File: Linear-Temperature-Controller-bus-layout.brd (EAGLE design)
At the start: 203.2 x 34.3 mm, 78 parts, among them IC1 LM393D, IC3 AD5624R, IC4 AD5262, IC5 LF356MX, T1 MMBT3904, T2 MMBT3904

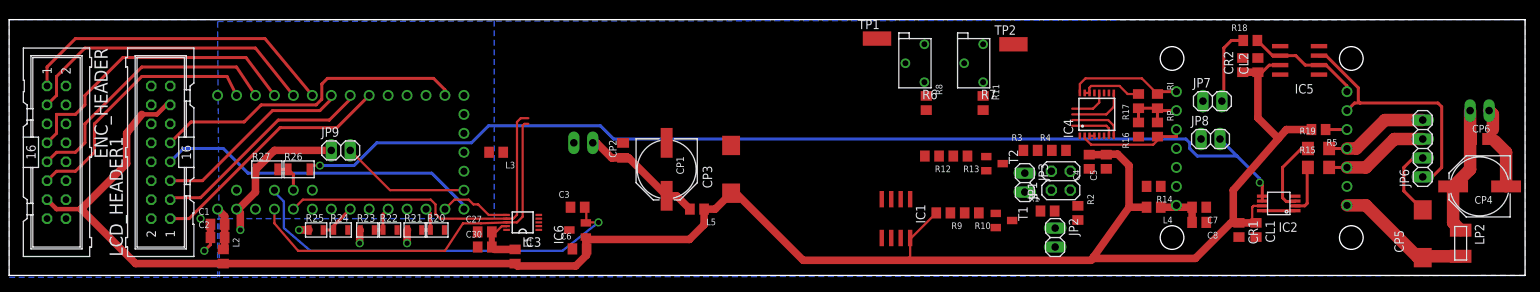
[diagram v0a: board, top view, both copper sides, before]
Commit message: Update BOM, continue laying out board
Also add a new board file to play around with having a bus of traces for
eventually extending the circuit to 4 channels
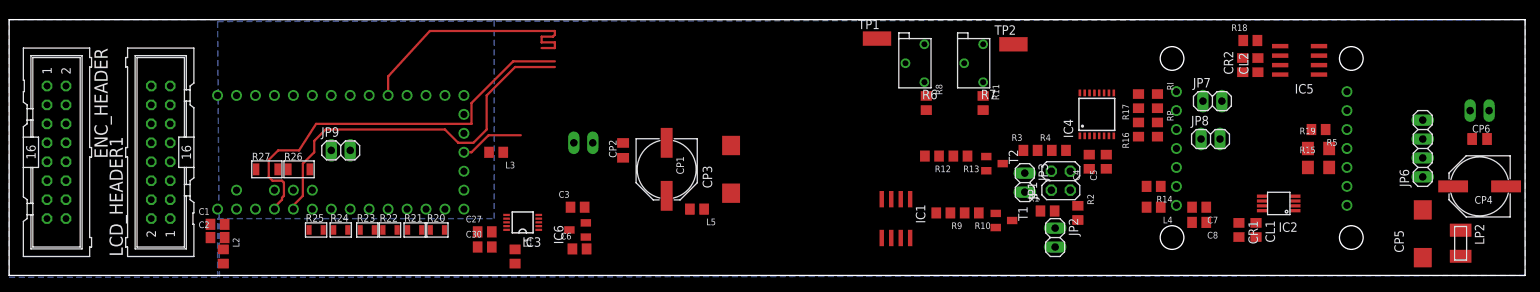
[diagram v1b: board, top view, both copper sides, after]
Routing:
- net VDD: track 267.0 -> 0.00 mm
- net VMON1: track 139.7 -> 0.00 mm, vias 2 -> 0
- net 2.5V: track 58.5 -> 0.00 mm, vias 1 -> 0
- net AGND: track 47.7 -> 0.00 mm, vias 4 -> 0
- net SCK: track 43.8 -> 0.00 mm
- net ENC_A2: track 43.2 -> 0.00 mm
- net MOSI: track 43.0 -> 0.00 mm
- net ENC_B2: track 40.7 -> 0.00 mm
- net ENC_A1: track 40.0 -> 0.00 mm
- net ENC_B1: track 36.7 -> 0.00 mm
- net ENC_SW1: track 35.0 -> 0.00 mm
- net N$13: track 33.7 -> 0.00 mm
- net RST_LCD: track 33.5 -> 0.00 mm
- net RS_LCD: track 30.2 -> 0.00 mm
- net CS_POT1: track 7.86 -> 35.0 mm
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
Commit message: Finished first attempt at board layout
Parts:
- added TP10, TP11, TP12, TP3, TP4, TP5, TP6, TP7, TP8, TP9: TESTPT, Lin-Temp-Controller:1206TESTPAD
- moved C4 57.5 mm to (156.0, -41.1)
- moved C5 57.5 mm to (158.2, -41.1)
- moved C8 57.5 mm to (170.7, -49.3)
- moved CL1 57.5 mm to (178.3, -50.3)
- moved CP4 57.5 mm to (208.3, -44.5)
- moved CP6 57.5 mm to (208.3, -38.1)
- moved CR1 57.5 mm to (176.0, -50.3)
- moved IC4 57.5 mm to (157.0, -34.8)
- moved JP1 57.5 mm to (152.1, -43.7)
- moved JP7 57.5 mm to (172.5, -33.0)
- moved JP8 57.5 mm to (172.2, -38.1)
- moved R1 57.5 mm to (150.4, -47.8)
- moved R11 57.5 mm to (141.7, -33.3)
- moved R12 57.5 mm to (134.9, -40.4)
- moved R13 57.5 mm to (138.7, -40.4)
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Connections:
- net 2.5V: now also TP12.P$1
- net ACT_T2: now also TP9.P$1
- net ACT_T3: now also TP10.P$1
- net ACT_T4: now also TP11.P$1
- net CS_POT2: now also TP3.P$1
- net CS_POT3: now also TP4.P$1
- net CS_POT4: now also TP5.P$1
- net VMON2: now also TP6.P$1
- net VMON3: now also TP7.P$1
- net VMON4: now also TP8.P$1
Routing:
- net CS_POT2: track 0.00 -> 245.3 mm
- net CS_POT3: track 0.00 -> 242.3 mm
- net CS_POT4: track 0.00 -> 236.3 mm
- net DGND: track 8.57 -> 241.0 mm
- net SCK_B: track 50.8 -> 274.2 mm
- net MOSI_B: track 54.6 -> 276.4 mm
- net CS_POT1: track 35.0 -> 247.7 mm
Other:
- board size 203.2 x 34.3 mm -> 304.8 x 34.3 mm
